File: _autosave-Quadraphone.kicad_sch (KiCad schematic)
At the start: 33 parts, among them J10 CV_IN, J11 CV_OUT, J7 Power_In, J8 Power_In, U1 AMS1117-5.0, U10 TL074, U2 MCP1501-25xSN, U3 DPDT_Switch, U4 LM4040DBZ-5, U5 MCP6002-xSN, U7 4066, U8 LM4040DBZ-2.5

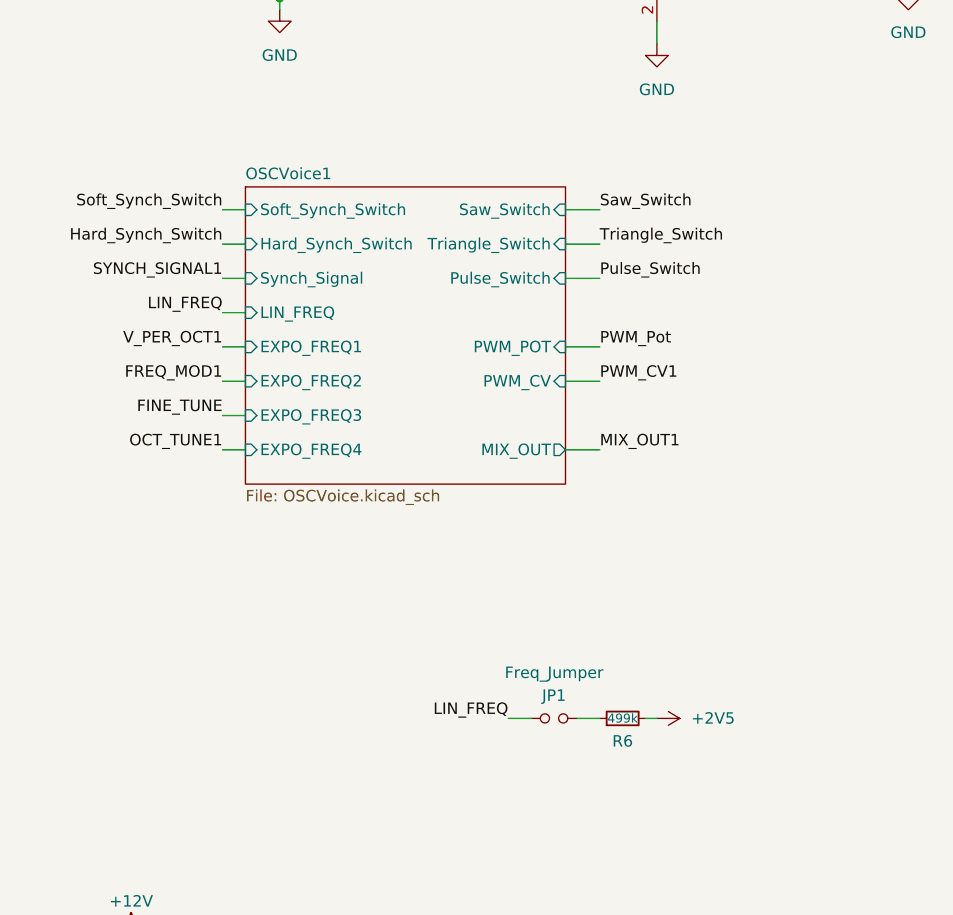
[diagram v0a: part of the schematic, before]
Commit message: Updates to linear frequency controls
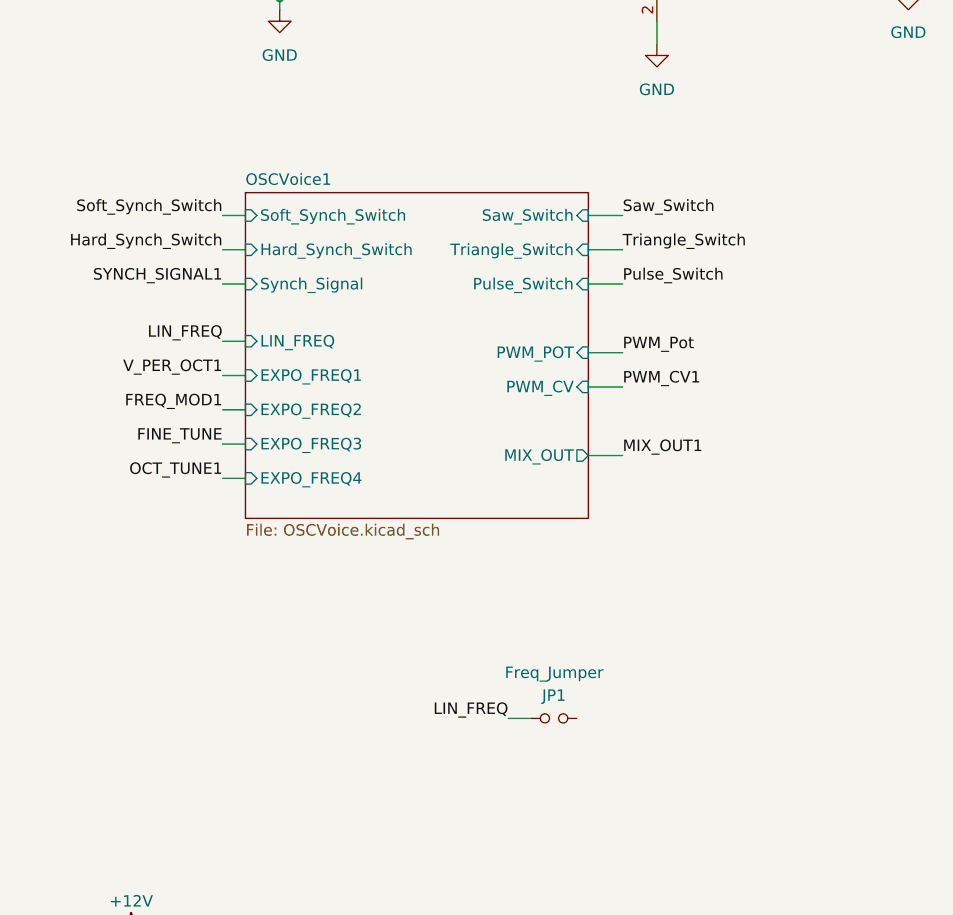
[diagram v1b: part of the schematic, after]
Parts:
- removed R6: 499k, Resistor_SMD:R_0805_2012Metric, symbol Device:R_Small
